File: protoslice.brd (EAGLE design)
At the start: 69 x 40 mm, 1 part

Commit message: Added initial components
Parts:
- added JP1, JP2, JP3, JP4, JP5, JP6, JP7, JP8, JP9: (no value), pinhead:2X14
- added SV1: (no value), con-lstb:MA10-2W
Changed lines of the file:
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@@
 <elements>
 <element name="U$1" library="amino" package="XSLICE" value="XSLICE" x="40.64" y="20.32"/>
+<element name="JP1" library="pinhead" package="2X14" value="" x="19.05" y="20.32" rot="R90"/>
+<element name="JP2" library="pinhead" package="2X14" value="" x="24.13" y="20.32" rot="R90"/>
+<element name="JP3" library="pinhead" package="2X14" value="" x="29.21" y="20.32" rot="R90"/>
+<element name="JP4" library="pinhead" package="2X14" value="" x="34.29" y="20.32" rot="R90"/>
+<element name="JP5" library="pinhead" package="2X14" value="" x="39.37" y="20.32" rot="R90"/>
+<element name="JP6" library="pinhead" package="2X14" value="" x="44.45" y="20.32" rot="R90"/>
+<element name="JP7" library="pinhead" package="2X14" value="" x="49.53" y="20.32" rot="R90"/>
+<element name="JP8" library="pinhead" package="2X14" value="" x="54.61" y="20.32" rot="R90"/>
+<element name="SV1" library="con-lstb" package="MA10-2W" value="" x="64.77" y="20.32" rot="R270">
+<attribute name="OC_NEWARK" value="unknown" x="64.77" y="20.32" size="1.778" layer="27" rot="R270" display="off"/>
+<attribute name="MPN" value="" x="64.77" y="20.32" size="1.778" layer="27" rot="R270" display="off"/>
+<attribute name="MF" value="" x="64.77" y="20.32" size="1.778" layer="27" rot="R270" display="off"/>
+<attribute name="OC_FARNELL" value="unknown" x="64.77" y="20.32" size="1.778" layer="27" rot="R270" display="off"/>
+</element>
+<element name="JP9" library="pinhead" package="2X14" value="" x="59.69" y="20.32" rot="R90"/>
 </elements>
 <signals>

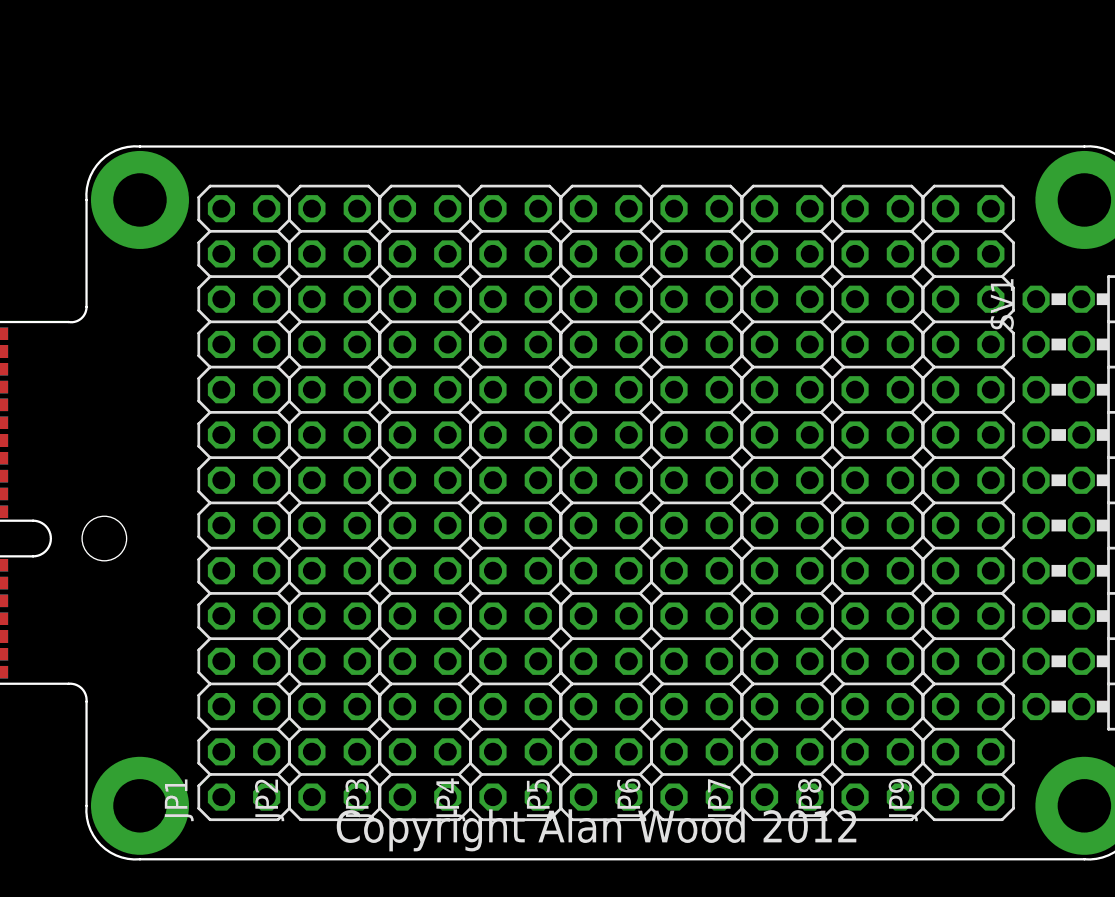
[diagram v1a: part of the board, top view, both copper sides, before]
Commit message: Added passive components
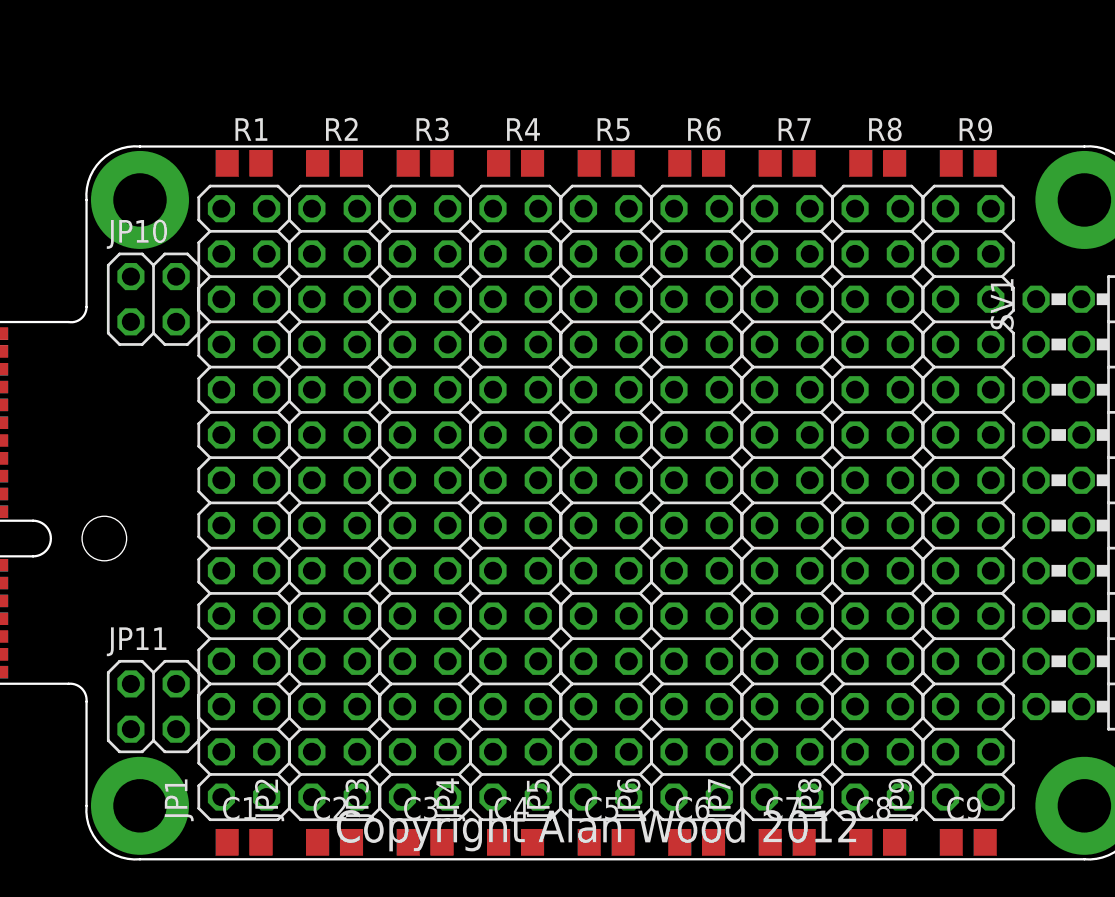
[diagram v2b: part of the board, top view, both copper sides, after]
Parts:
- added C1, C2, C3, C4, C5, C6, C7, C8, C9: (no value), rcl:C0805
- added JP10, JP11: (no value), pinhead:2X02
- added R1, R2, R3, R4, R5, R6, R7, R8, R9: (no value), rcl:R0805
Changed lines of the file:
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@@
 <layer number="23" name="tOrigins" color="15" fill="1" visible="yes" active="yes"/>
 <layer number="24" name="bOrigins" color="15" fill="1" visible="yes" active="yes"/>
-<layer number="25" name="tNames" color="7" fill="1" visible="yes" active="yes"/>
-<layer number="26" name="bNames" color="7" fill="1" visible="yes" active="yes"/>
-<layer number="27" name="tValues" color="7" fill="1" visible="yes" active="yes"/>
-<layer number="28" name="bValues" color="7" fill="1" visible="yes" active="yes"/>
+<layer number="25" name="tNames" color="7" fill="1" visible="no" active="yes"/>
+<layer number="26" name="bNames" color="7" fill="1" visible="no" active="yes"/>
+<layer number="27" name="tValues" color="7" fill="1" visible="no" active="yes"/>
+<layer number="28" name="bValues" color="7" fill="1" visible="no" active="yes"/>
 <layer number="29" name="tStop" color="7" fill="3" visible="no" active="yes"/>
 <layer number="30" name="bStop" color="7" fill="6" visible="no" active="yes"/>
@@
 </element>
 <element name="JP9" library="pinhead" package="2X14" value="" x="59.69" y="20.32" rot="R90"/>
+<element name="JP10" library="pinhead" package="2X02" value="" x="13.97" y="31.75"/>
+<element name="JP11" library="pinhead" package="2X02" value="" x="13.97" y="8.89"/>
+<element name="R1" library="rcl" package="R0805" value="" x="19.05" y="39.37"/>
+<element name="R2" library="rcl" package="R0805" value="" x="24.13" y="39.37"/>
+<element name="R3" library="rcl" package="R0805" value="" x="29.21" y="39.37"/>
+<element name="R4" library="rcl" package="R0805" value="" x="34.29" y="39.37"/>
+<element name="R5" library="rcl" package="R0805" value="" x="39.37" y="39.37"/>
+<element name="R6" library="rcl" package="R0805" value="" x="44.45" y="39.37"/>
+<element name="R7" library="rcl" package="R0805" value="" x="49.53" y="39.37"/>
+<element name="R8" library="rcl" package="R0805" value="" x="54.61" y="39.37"/>
+<element name="R9" library="rcl" package="R0805" value="" x="59.69" y="39.37"/>
+<element name="C1" library="rcl" package="C0805" value="" x="19.05" y="1.27"/>
+<element name="C2" library="rcl" package="C0805" value="" x="24.13" y="1.27"/>
+<element name="C3" library="rcl" package="C0805" value="" x="29.21" y="1.27"/>
+<element name="C4" library="rcl" package="C0805" value="" x="34.29" y="1.27"/>
+<element name="C5" library="rcl" package="C0805" value="" x="39.37" y="1.27"/>
+<element name="C6" library="rcl" package="C0805" value="" x="44.45" y="1.27"/>
+<element name="C7" library="rcl" package="C0805" value="" x="49.53" y="1.27"/>
+<element name="C8" library="rcl" package="C0805" value="" x="54.61" y="1.27"/>
+<element name="C9" library="rcl" package="C0805" value="" x="59.69" y="1.27"/>
 </elements>
 <signals>

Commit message: Made for energy monitor proto
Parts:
- removed C1: (no value), rcl:C0805
- removed R1: (no value), rcl:R0805
- moved C2 38.1 mm to (24.1, 39.4), turned to 180 degrees
- moved C3 38.1 mm to (29.2, 39.4), turned to 180 degrees
- moved C4 38.1 mm to (34.3, 39.4), turned to 180 degrees
- moved C5 38.1 mm to (39.4, 39.4), turned to 180 degrees
- moved C6 38.1 mm to (44.5, 39.4), turned to 180 degrees
- moved C7 38.1 mm to (49.5, 39.4), turned to 180 degrees
- moved C8 38.1 mm to (54.6, 39.4), turned to 180 degrees
- moved C9 38.1 mm to (59.7, 39.4), turned to 180 degrees
- moved R2 38.1 mm to (24.1, 1.27), turned to 180 degrees
- moved R3 38.1 mm to (29.2, 1.27), turned to 180 degrees
- moved R4 38.1 mm to (34.3, 1.27), turned to 180 degrees
- moved R5 38.1 mm to (39.4, 1.27), turned to 180 degrees
- moved R6 38.1 mm to (44.5, 1.27), turned to 180 degrees
- moved R7 38.1 mm to (49.5, 1.27), turned to 180 degrees
- moved R8 38.1 mm to (54.6, 1.27), turned to 180 degrees
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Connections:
- new net A1: JP11.1, U$1.A1
- new net A11: JP1.17, U$1.A11
- new net A12: JP1.19, U$1.A12
- new net A13: JP1.21, U$1.A13
- new net A15: JP1.25, U$1.A15
- new net A16: JP1.27, U$1.A16
- new net A17: JP10.1, U$1.A17
- new net A18: JP10.3, U$1.A18
- new net A3: JP1.1, U$1.A3
- new net A4: JP1.3, U$1.A4
- new net A5: JP1.5, U$1.A5
- new net A6: JP1.7, U$1.A6
- new net A7: JP1.9, U$1.A7
- new net A8: JP1.11, U$1.A8
- new net A9: JP1.13, U$1.A9
- new net B1: JP11.2, U$1.B1
- new net B10: JP1.16, U$1.B10
- new net B11: JP1.18, U$1.B11
- new net B12: JP1.20, U$1.B12
- new net B13: JP1.22, U$1.B13
- new net B14: JP1.24, U$1.B14
- new net B15: JP1.26, U$1.B15
- new net B17: JP10.2, U$1.B17
- new net B18: JP10.4, U$1.B18
- new net B2: JP11.4, U$1.B2
- new net B4: JP1.4, U$1.B4
- new net B6: JP1.8, U$1.B6
- new net B7: JP1.10, U$1.B7
- new net B9: JP1.14, U$1.B9
- new net N$1: JP2.1, R2.1
- new net N$10: JP5.2, R5.2
- new net N$11: JP6.1, R6.1
- new net N$12: JP6.2, R6.2
- new net N$13: JP7.1, R7.1
- new net N$14: JP7.2, R7.2
- new net N$15: C7.1, JP7.27
- new net N$16: C7.2, JP7.28
- new net N$17: C6.2, JP6.28
- new net N$18: C6.1, JP6.27
- new net N$19: C5.2, JP5.28
- new net N$2: JP2.2, R2.2
- new net N$20: C5.1, JP5.27
- new net N$21: C4.2, JP4.28
- new net N$22: C4.1, JP4.27
- new net N$23: C3.2, JP3.28
- new net N$24: C3.1, JP3.27
- new net N$25: JP8.1, R8.1
- new net N$26: JP8.2, R8.2
- new net N$27: C8.1, JP8.27
- new net N$28: C8.2, JP8.28
- new net N$29: C9.1, JP9.27
- new net N$3: C2.1, JP2.27
- new net N$30: C9.2, JP9.28
- new net N$31: JP9.1, R9.1
- new net N$32: JP9.2, R9.2
- new net N$4: C2.2, JP2.28
- new net N$5: JP3.1, R3.1
- new net N$6: JP3.2, R3.2
- new net N$7: JP4.1, R4.1
- new net N$8: JP4.2, R4.2
- new net N$9: JP5.1, R5.1
- new net O1: JP9.5, SV1.20
- new net O10: JP9.23, SV1.2
- new net O11: JP9.6, SV1.19
- new net O12: JP9.8, SV1.17
- new net O13: JP9.10, SV1.15
- new net O14: JP9.12, SV1.13
- new net O15: JP9.14, SV1.11
- new net O16: JP9.16, SV1.9
- new net O17: JP9.18, SV1.7
- new net O18: JP9.20, SV1.5
- new net O19: JP9.22, SV1.3
- new net O2: JP9.7, SV1.18
- new net O20: JP9.24, SV1.1
- new net O3: JP9.9, SV1.16
- new net O4: JP9.11, SV1.14
- new net O5: JP9.13, SV1.12
- new net O6: JP9.15, SV1.10
- new net O7: JP9.17, SV1.8
- new net O8: JP9.19, SV1.6
- new net O9: JP9.21, SV1.4
- net A10: now also JP1.15
- net A14: now also JP1.23
- net A2: now also JP11.3
- net B16: now also JP1.28
- net B3: now also JP1.2
- net B5: now also JP1.6
- net B8: now also JP1.12
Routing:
- net B16: track 0.00 -> 23.6 mm
- net B3: track 0.00 -> 23.6 mm
- net B15: track 0.00 -> 22.1 mm
- net B4: track 0.00 -> 22.1 mm
- net B5: track 0.00 -> 20.3 mm
- net B14: track 0.00 -> 20.3 mm
- net A3: track 0.00 -> 20.2 mm
- net A16: track 0.00 -> 20.2 mm
- net B6: track 0.00 -> 19.3 mm
- net B13: track 0.00 -> 19.3 mm
- net A15: track 0.00 -> 19.2 mm
- net A4: track 0.00 -> 19.2 mm
- net B11: track 0.00 -> 18.3 mm
- net B12: track 0.00 -> 17.8 mm
- net B7: track 0.00 -> 17.8 mm
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
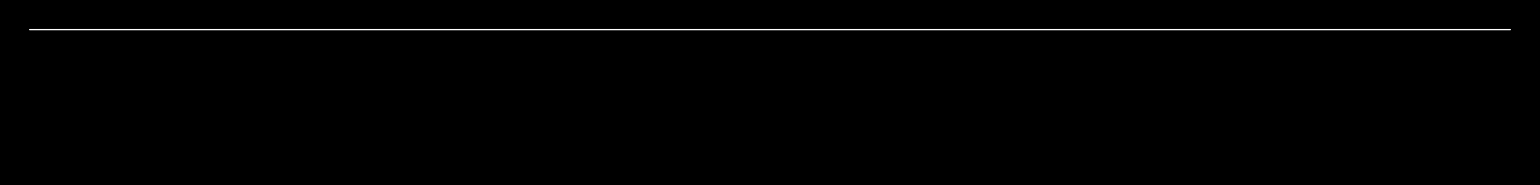
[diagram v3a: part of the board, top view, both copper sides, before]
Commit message: removed random line
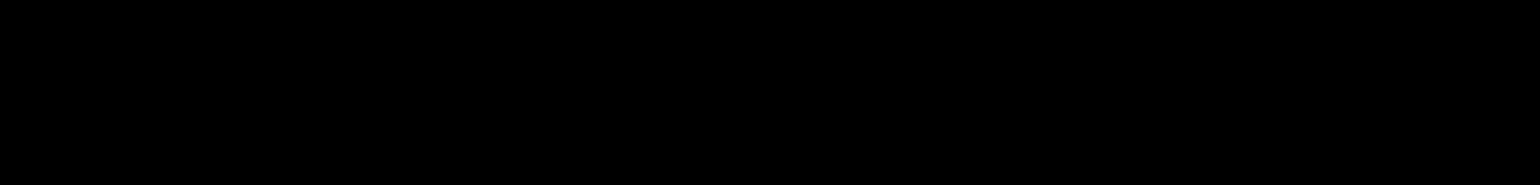
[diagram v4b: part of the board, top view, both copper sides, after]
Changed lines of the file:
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@@
 <board>
 <plain>
-<wire x1="100" y1="80" x2="0" y2="80" width="0" layer="20"/>
 <text x="24.13" y="1.27" size="1.778" layer="25">Copyright Alan Wood 2012</text>
 </plain>
